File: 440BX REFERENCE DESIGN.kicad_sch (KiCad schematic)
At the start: 0 parts

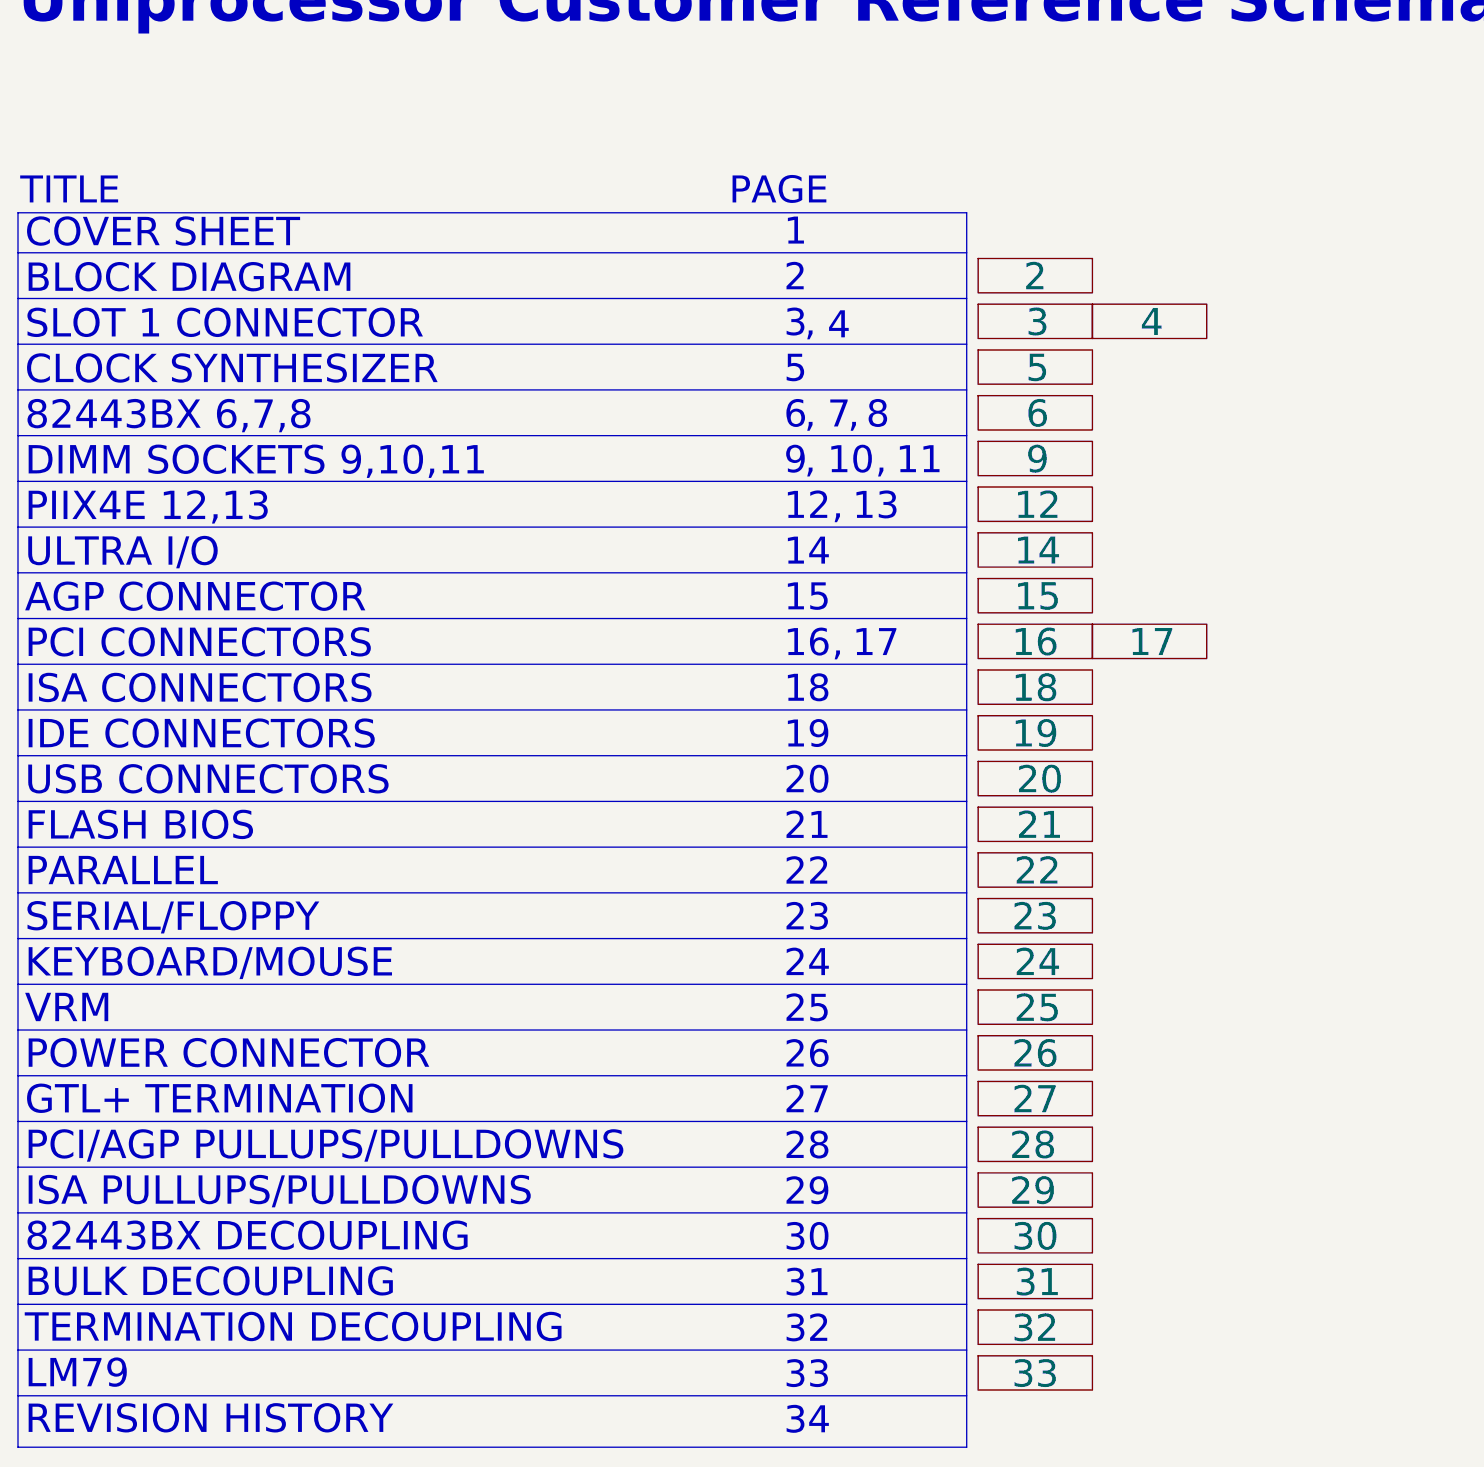
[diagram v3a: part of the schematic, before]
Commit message: pages 9 10 11 DIMM socket and DIMM socket symbol
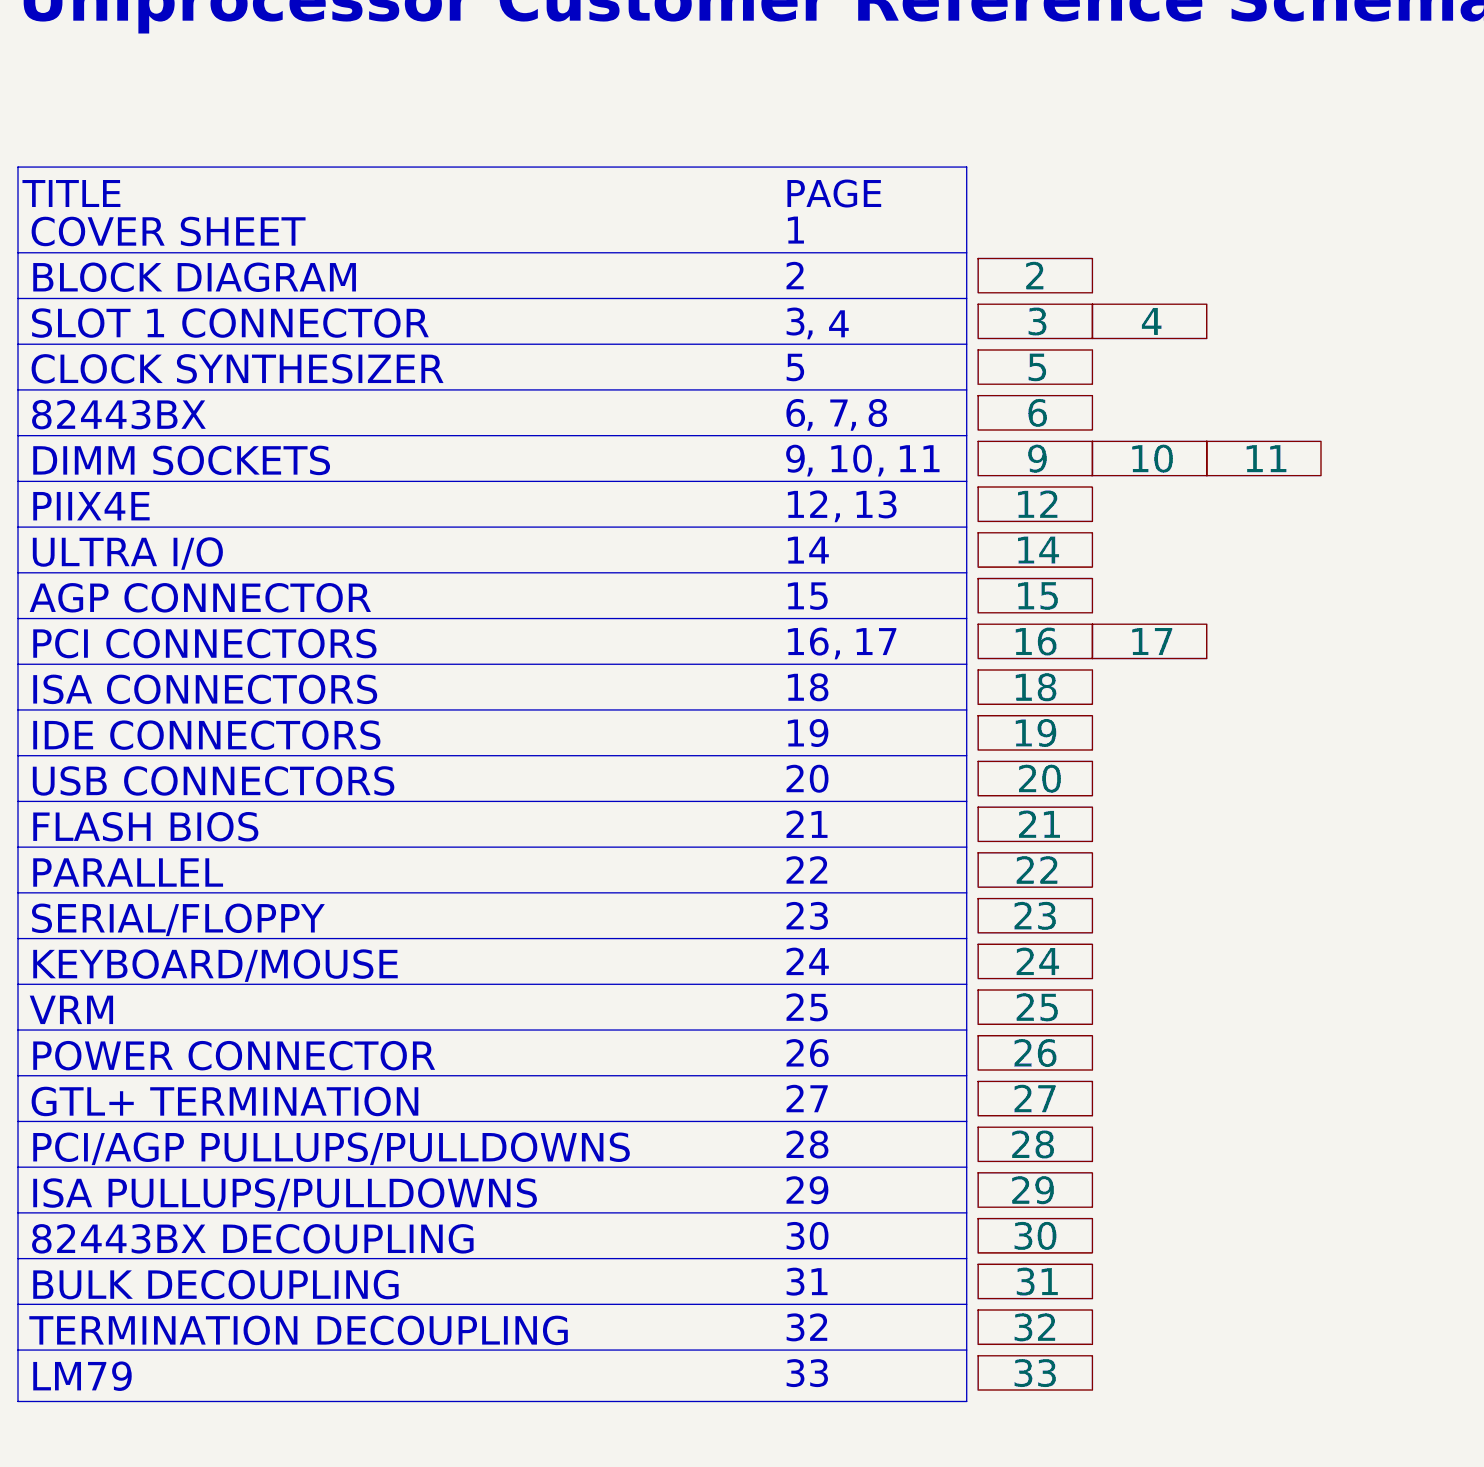
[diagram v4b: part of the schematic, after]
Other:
- sheet DIMM SOCKETS renamed DIMM SOCKET 0
- added sheet DIMM SOCKET 1 (DIMM SOCKET1.kicad_sch)
- added sheet DIMM SOCKET 2 (DIMM SOCKET2.kicad_sch)
- sheet DIMM SOCKET 0: file DIMM SOCKETS.kicad_sch -> DIMM SOCKET0.kicad_sch
- note added: "COVER SHEET BLOCK DIAGRAM SLOT 1 CONNECTOR CLOCK SYNTHESIZER 82443BX DIMM SOCKETS PIIX4E ULTRA I/O AGP CONNECTOR PCI CONNECTORS ISA CONNECTORS IDE CONNECTORS USB CONNECTORS FLASH BIOS PARALLEL SERIAL/FLOPPY KEYBOARD/MOUSE VRM POWER CONNECTOR GTL+ TERMINATION PCI/AGP PULLUPS/PULLDOWNS ISA PULLUPS/PULLDOWNS 82443BX DECOUPLING BULK DECOUPLING TERMINATION DECOUPLING LM79"
- note removed: "34"
- note removed: "COVER SHEET BLOCK DIAGRAM SLOT 1 CONNECTOR CLOCK SYNTHESIZER 82443BX 6,7,8 DIMM SOCKETS 9,10,11 PIIX4E 12,13 ULTRA I/O AGP CONNECTOR PCI CONNECTORS ISA CONNECTORS IDE CONNECTORS USB CONNECTORS FLASH BIOS PARALLEL SERIAL/FLOPPY KEYBOARD/MOUSE VRM POWER CONNECTOR GTL+ TERMINATION PCI/AGP PULLUPS/PULLDOWNS ISA PULLUPS/PULLDOWNS 82443BX DECOUPLING BULK DECOUPLING TERMINATION DECOUPLING LM79 REVISION 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"
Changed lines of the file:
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@@
 	)
 	(rectangle
-		(start 29.21 52.07)
-		(end 134.62 189.23)
+		(start 29.21 46.99)
+		(end 134.62 184.15)
 		(stroke
 			(width 0)
@@
 	(text "PAGE"
 		(exclude_from_sim no)
-		(at 108.204 49.784 0)
+		(at 114.3 50.292 0)
 		(effects
 			(font
@@
 		)
 	)
-	(text "COVER SHEET\nBLOCK DIAGRAM\nSLOT 1 CONNECTOR\nCLOCK SYNTHESIZER\n82443BX 6,7,8\nDIMM SOCKETS 9,10,11\nPIIX4E 12,13\nULTRA I/O\nAGP CONNECTOR\nPCI CONNECTORS\nISA CONNECTORS\nIDE CONNECTORS\nUSB CONNECTORS\nFLASH BIOS\nPARALLEL\nSERIAL/FLOPPY\nKEYBOARD/MOUSE\nVRM\nPOWER CONNECTOR\nGTL+ TERMINATION\nPCI/AGP PULLUPS/PULLDOWNS\nISA PULLUPS/PULLDOWNS\n82443BX DECOUPLING\nBULK DECOUPLING\nTERMINATION DECOUPLING\nLM79\nREVISION HISTORY\n"
-		(exclude_from_sim no)
-		(at 29.972 120.396 0)
-		(effects
-			(font
-				(size 3.15 3.15)
+	(text "COVER SHEET\nBLOCK DIAGRAM\nSLOT 1 CONNECTOR\nCLOCK SYNTHESIZER\n82443BX\nDIMM SOCKETS\nPIIX4E\nULTRA I/O\nAGP CONNECTOR\nPCI CONNECTORS\nISA CONNECTORS\nIDE CONNECTORS\nUSB CONNECTORS\nFLASH BIOS\nPARALLEL\nSERIAL/FLOPPY\nKEYBOARD/MOUSE\nVRM\nPOWER CONNECTOR\nGTL+ TERMINATION\nPCI/AGP PULLUPS/PULLDOWNS\nISA PULLUPS/PULLDOWNS\n82443BX DECOUPLING\nBULK DECOUPLING\nTERMINATION DECOUPLING\nLM79"
+		(exclude_from_sim no)
+		(at 30.48 118.11 0)
+		(effects
+			(font
+				(size 3.16 3.16)
 				(color 0 0 0 1)
 			)
@@
 		)
 	)
-	(text "34"
-		(exclude_from_sim no)
-		(at 114.3 186.436 0)
-		(effects
-			(font
-				(size 3 3)
-			)
-			(justify left)
-			(href "#34")
-		)
-	)
 	(text "31"
 		(exclude_from_sim no)
@@
 	(text "TITLE"
 		(exclude_from_sim no)
-		(at 29.464 49.784 0)
+		(at 29.718 50.292 0)
 		(effects
 			(font
@@
 	(polyline
 		(pts
-			(xy 29.21 183.515) (xy 134.62 183.515)
-		)
-		(stroke
-			(width 0)
-			(type default)
-			(color 0 0 0 1)
-		)
-	)
-	(polyline
-		(pts
 			(xy 29.21 153.035) (xy 134.62 153.035)
 		)
@@
 	)
 	(sheet
+		(at 148.59 77.47)
+		(size 12.7 3.81)
+		(exclude_from_sim no)
+		(in_bom yes)
+		(on_board yes)
+		(dnp no)
+		(stroke
+			(width 0.1524)
+			(type solid)
+		)
+		(fill
+			(color 0 0 0 0.0000)
+		)
+		(property "Sheetname" "DIMM SOCKET 1"
+			(at 148.59 76.7584 0)
+			(effects
+				(font
+					(size 1.27 1.27)
+				)
+				(justify left bottom)
+				(hide yes)
+			)
+		)
+		(property "Sheetfile" "DIMM SOCKET1.kicad_sch"
+			(at 148.59 81.8646 0)
+			(effects
+				(font
+					(size 1.27 1.27)
+				)
+				(justify left top)
+				(hide yes)
+			)
+		)
+		(property "page" "10"
+			(at 155.194 79.502 0)
+			(effects
+				(font
+					(size 3 3)
+					(color 0 0 0 1)
+				)
+			)
+		)
+		(instances
+			(project "440BX REFERENCE DESIGN"
+				(path "/373c3af7-3bc7-49b4-93d6-3114ef59c408"
+					(page "10")
+				)
+			)
+		)
+	)
+	(sheet
 		(at 135.89 168.91)
 		(size 12.7 3.81)
@@
 			(color 0 0 0 0.0000)
 		)
-		(property "Sheetname" "DIMM SOCKETS"
+		(property "Sheetname" "DIMM SOCKET 0"
 			(at 136.144 81.28 0)
 			(effects
@@
 			)
 		)
-		(property "Sheetfile" "DIMM SOCKETS.kicad_sch"
+		(property "Sheetfile" "DIMM SOCKET0.kicad_sch"
 			(at 135.89 81.8646 0)
 			(effects
@@
 				(path "/373c3af7-3bc7-49b4-93d6-3114ef59c408"
 					(page "22")
+				)
+			)
+		)
+	)
+	(sheet
+		(at 161.29 77.47)
+		(size 12.7 3.81)
+		(exclude_from_sim no)
+		(in_bom yes)
+		(on_board yes)
+		(dnp no)
+		(stroke
+			(width 0.1524)
+			(type solid)
+		)
+		(fill
+			(color 0 0 0 0.0000)
+		)
+		(property "Sheetname" "DIMM SOCKET 2"
+			(at 161.29 76.7584 0)
+			(effects
+				(font
+					(size 1.27 1.27)
+				)
+				(justify left bottom)
+				(hide yes)
+			)
+		)
+		(property "Sheetfile" "DIMM SOCKET2.kicad_sch"
+			(at 161.29 81.8646 0)
+			(effects
+				(font
+					(size 1.27 1.27)
+				)
+				(justify left top)
+				(hide yes)
+			)
+		)
+		(property "page" "11"
+			(at 167.894 79.502 0)
+			(effects
+				(font
+					(size 3 3)
+					(color 0 0 0 1)
+				)
+			)
+		)
+		(instances
+			(project "440BX REFERENCE DESIGN"
+				(path "/373c3af7-3bc7-49b4-93d6-3114ef59c408"
+					(page "11")
 				)
 			)
@@
 			(name "440BX REFERENCE DESIGN.kicad_wks")
 			(type worksheet)
-			(data |KLUv/WDlB40SAAZcVyDwGD3QMXKnXDsbi32DJuszM1YDozZwAa5Ts8AzOG+fCk8ARwBRAB8C2Rxl
-				XwvKtfP8xzkDlTB26Ddr8ms5A4WyPWW/P/kXAICAwCO9f4sFxCyPZTf3cJ7VGX/Nfh1kwKSUiBln
-				X2y/7KUCICD4RibPVjU7KgSeJa3+k3/2NCLo7EhRp6xd+9U9z9lvxtpzHTtaIw1zWTv39ttD39sl
-				4Vzb6r/edVibPXu73lHK/lz/s6z2rt7XPHf4H2ceDtVygVgaFk9ZzKIVFE5KRYKRbCCX22GU/CKj
-				pB5+Cq+OcgXJNB4eiAaDkagI3c3wr4+cMyr7X9ca9bH/kUR0tmygJu2YZVmUiALgL/7IprM/HAGB
-				AVNARWMJmFi8f5ZIozmOeF1tuBQ4/yvp28medSQKScMUg3PKCSlNSBijZrn6tiGTjCTDvc1stq/G
-				LnjRQR96NehmvHvI6q9dxp/O7gVmoCE9pJQiEilIkkI6YGTExqobNwSlNVRTpI+GWluUtzbAf5mA
-				30RDIVnOD/bYCZAulz/3q5O2kVtoSPgu+vVJtuwApwIAk70iciO5ou0cAi0kC9d0sDAIJSAZgDDG
-				iYGlMcsbgByPt3DRgvjhABywoz82hwwFBYQRGmrqiWpFYSry2VMukazjaK2hOyAI0ZzSn6hW9sIx
-				fLDbh5+HdQEyi7BwCx3/0ivTjet5tAkCmklFQkpQU4sX+pAw7vokDvlQsBc9TL8aIBzYiABIRMps
-				0UG6bUkZbEigc7xi79OhqU7qw7oeCA6XuKmcNCAdg1cF|
-			)
-			(checksum "AEDEA97BEAD93D669076F0EFF005E131")
-		)
-	)
+			(data |KLUv/WD2B9USAKabViDwGD3QMXKnXDsbi32DJuszM1YDo41yAa5Ts8AzOG+fCk4ARgBQACGQzVH2
+				taBcO89/nDNQCWOHfrMmv5YzUCjbU/b7k38BAAgIPNL7t1hAzPJYdnMP51md8dfs10EGTEp5zTj7
+				YvtlLxUAAcE3Mnm2qtlRIX/yz57Gi86OFHXK2rVf3fOc/WasPdexozXSMJe1c2+/PfS9XRLOta3+
+				612Htdmzt+tNE/CKsj/X/yyrvav3Nc8d/seZhz8WT1nMohUUTkpFgpFsIJfbYZT8IqOkHn4KEY1d
+				cMYVJNN4eCAaDEaiInQ3w78+cs6o7H9da9TH/kcS0dmygZq0Y5ZlUV4FwF/8mf1hz5JWBwGBAVNA
+				RSegXLx/lkijOY6IQLThUuD8ryR71pEoJA3TOROYxOC10CxX3zZkkpFkuLeZzTaiLwkxxKAPvRp0
+				M949ZPXXLuNPZ/eq5QKxNAJsoBE9pZQiEilIkkI6UMSQGjRuNATPNl2DpDiM1Q0JLilvYcgX5q3F
+				KnoTDhZl/DssY9ijeoBsck67n65kc8Ky+vvfzLHaxyHTziGOCAChf4Xkdnp127tFWHgWpwXgCawq
+				gApMFhBmbpwByyeWFxB9rz1x16l5frhLwFKSZnjLZ1BAGKCjTj3QoSwmLFd7ymUk6gBabGkPCGI0
+				5ylvFCl67wQu6P0TjtViAZnKrKzTDQLOK29NW9fxaRMGmlFNUiowVAsr0AFB7jpJndJgsRQ90l4l
+				fDg5okEQJGmi8CShxbysduTwE79j71OiTZ3fh3U9WBw+4n5y0oF0DEwV|
+			)
+			(checksum "9CDFC081BFE7BE9B5ADA55881BA639E9")
+		)
+	)

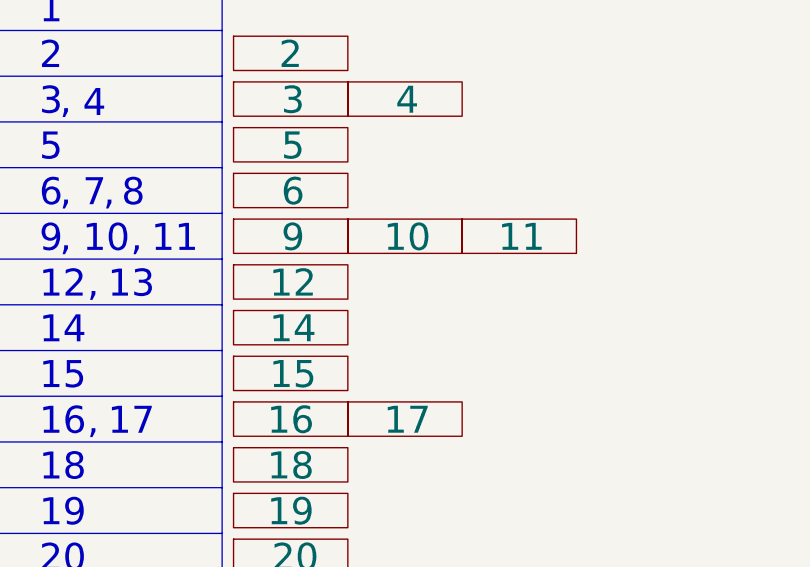
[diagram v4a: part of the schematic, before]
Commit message: Pages 12 13 PIIX4E done
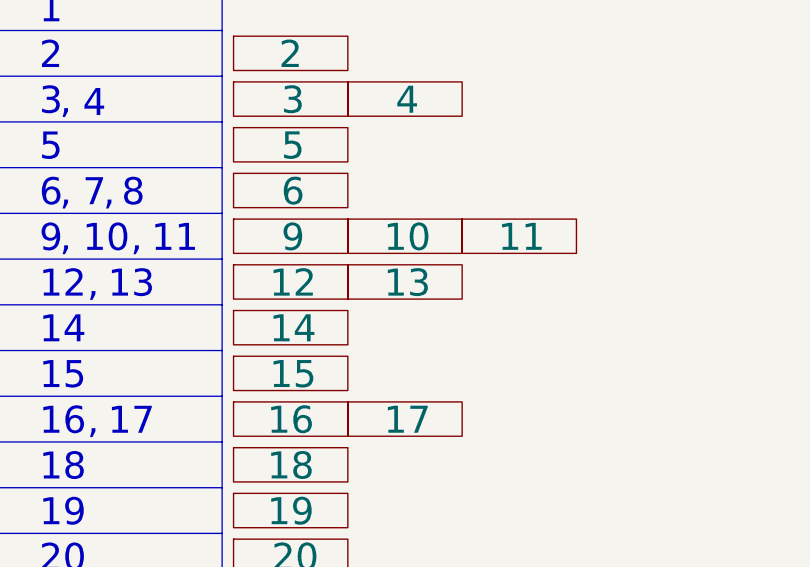
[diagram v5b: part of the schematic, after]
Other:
- sheet PII4XE renamed 82371EB (PART I)
- added sheet 82371EB (PART II) (82371EB2.kicad_sch)
- sheet 82371EB (PART I): file PII4XE.kicad_sch -> 82371EB1.kicad_sch
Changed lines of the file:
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@@
+	)
+	(sheet
+		(at 148.59 82.55)
+		(size 12.7 3.81)
+		(exclude_from_sim no)
+		(in_bom yes)
+		(on_board yes)
+		(dnp no)
+		(stroke
+			(width 0.1524)
+			(type solid)
+			(color 0 0 0 1)
+		)
+		(fill
+			(color 0 0 0 0.0000)
+		)
+		(property "Sheetname" "82371EB (PART II)"
+			(at 148.59 81.8384 0)
+			(effects
+				(font
+					(size 1.27 1.27)
+				)
+				(justify left bottom)
+				(hide yes)
+			)
+		)
+		(property "Sheetfile" "82371EB2.kicad_sch"
+			(at 148.59 86.9446 0)
+			(effects
+				(font
+					(size 1.27 1.27)
+				)
+				(justify left top)
+				(hide yes)
+			)
+		)
+		(property "page" "13"
+			(at 155.194 84.582 0)
+			(effects
+				(font
+					(size 3 3)
+					(color 0 0 0 1)
+				)
+			)
+		)
+		(instances
+			(project "440BX REFERENCE DESIGN"
+				(path "/373c3af7-3bc7-49b4-93d6-3114ef59c408"
+					(page "13")
+				)
+			)
+		)
 	)
 	(sheet
@@
 			(color 0 0 0 0.0000)
 		)
-		(property "Sheetname" "PII4XE"
+		(property "Sheetname" "82371EB (PART I)"
 			(at 136.144 86.36 0)
 			(effects
@@
 			)
 		)
-		(property "Sheetfile" "PII4XE.kicad_sch"
+		(property "Sheetfile" "82371EB1.kicad_sch"
 			(at 135.89 86.9446 0)
 			(effects
